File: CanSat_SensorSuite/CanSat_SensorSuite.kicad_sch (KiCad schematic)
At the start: 0 parts

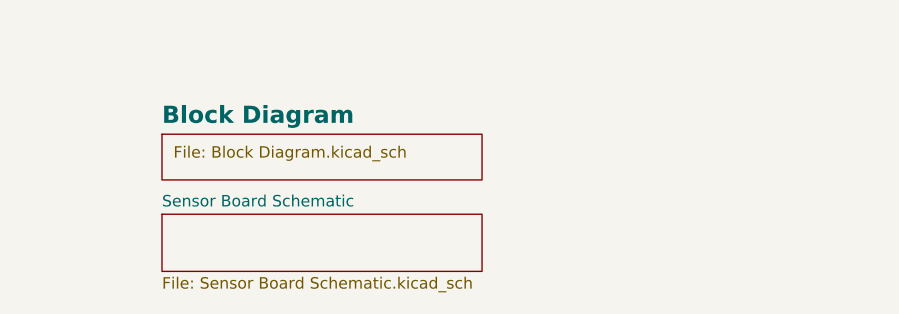
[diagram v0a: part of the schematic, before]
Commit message: Minor schematic changes
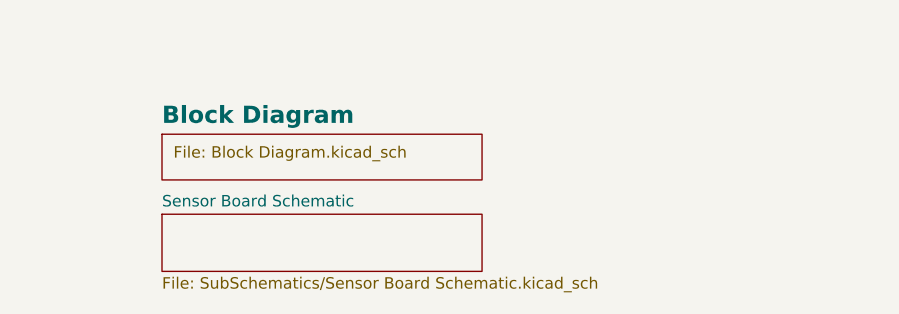
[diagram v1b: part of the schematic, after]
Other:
- sheet Sensor Board Schematic: file Sensor Board Schematic.kicad_sch -> SubSchematics/Sensor Board Schematic.kicad_sch
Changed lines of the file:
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@@
 			)
 		)
-		(property "Sheetfile" "Sensor Board Schematic.kicad_sch"
+		(property "Sheetfile" "SubSchematics/Sensor Board Schematic.kicad_sch"
 			(at 299.72 318.0846 0)
 			(effects

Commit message: Example files update
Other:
- added sheet Block DiagramSULREexample (Block DiagramSULREexample.kicad_sch)
- note added: "Add extra bright LED for visibility through body tube?"
- note added: "Add/confirm Atmo Sensors"
- note added: "Add/confirm Position Sensors"
- note added: "Atmospheric Sensors"
- note added: "Make block diagram"
- note added: "Positioning Sensors"
- note added: "To Do:"
- note removed: "21"
- note removed: "22"
- note removed: "23"
- note removed: "24"
- note removed: "25"
- note removed: "26"
- note removed: "27"
- note removed: "28"
- note removed: "29"
- note removed: "30"
- note removed: "31"
- note removed: "32"
- note removed: "33"
- note removed: "34"
- note removed: "35"
- note removed: "36"
- note removed: "37"
- note removed: "38"
- note removed: "39"
- note removed: "40"

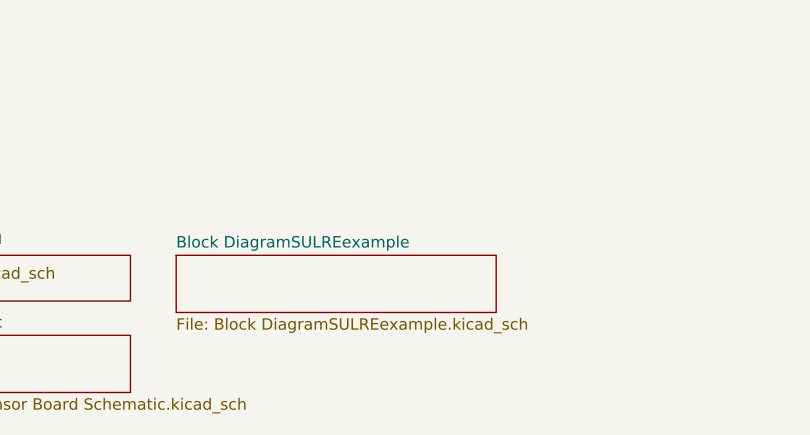
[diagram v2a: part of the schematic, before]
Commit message: Minor schematic adjustments
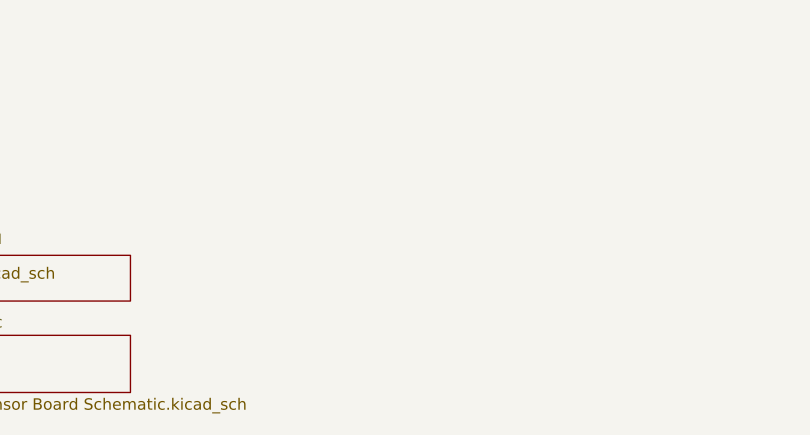
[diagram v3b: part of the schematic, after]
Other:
- removed sheet Block DiagramSULREexample
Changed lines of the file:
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@@
-	)
-	(sheet
-		(at 340.36 302.26)
-		(size 35.56 6.35)
-		(exclude_from_sim no)
-		(in_bom yes)
-		(on_board yes)
-		(dnp no)
-		(fields_autoplaced yes)
-		(stroke
-			(width 0.1524)
-			(type solid)
-		)
-		(fill
-			(color 0 0 0 0.0000)
-		)
-		(property "Sheetname" "Block DiagramSULREexample"
-			(at 340.36 301.5484 0)
-			(effects
-				(font
-					(size 1.27 1.27)
-				)
-				(justify left bottom)
-			)
-		)
-		(property "Sheetfile" "Block DiagramSULREexample.kicad_sch"
-			(at 340.36 309.1946 0)
-			(effects
-				(font
-					(size 1.27 1.27)
-				)
-				(justify left top)
-			)
-		)
-		(instances
-			(project "CanSat_SensorSuite"
-				(path "/0650c7a8-acba-429c-9f8e-eec0baf0bc1c"
-					(page "9")
-				)
-			)
-		)
 	)
 	(sheet
